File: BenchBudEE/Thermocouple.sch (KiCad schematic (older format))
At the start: 0 parts

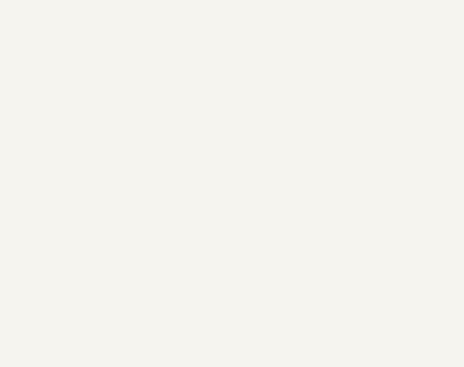
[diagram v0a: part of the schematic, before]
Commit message: Added initial module I/O
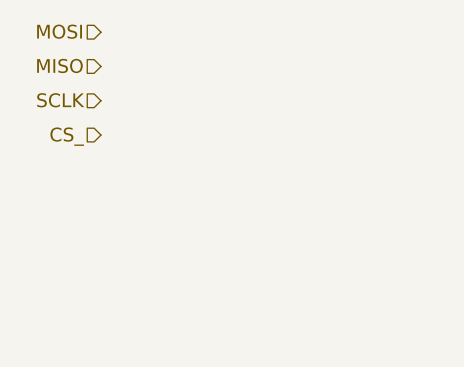
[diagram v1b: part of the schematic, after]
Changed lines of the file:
@@
 Text HLabel 9450 2900 2    60   Input ~ 0
 TC IN-
+Text HLabel 1300 1700 0    60   Input ~ 0
+MISO
+Text HLabel 1300 1550 0    60   Input ~ 0
+MOSI
+Text HLabel 1300 1850 0    60   Input ~ 0
+SCLK
+Text HLabel 1300 2000 0    60   Input ~ 0
+CS_
 $EndSCHEMATC

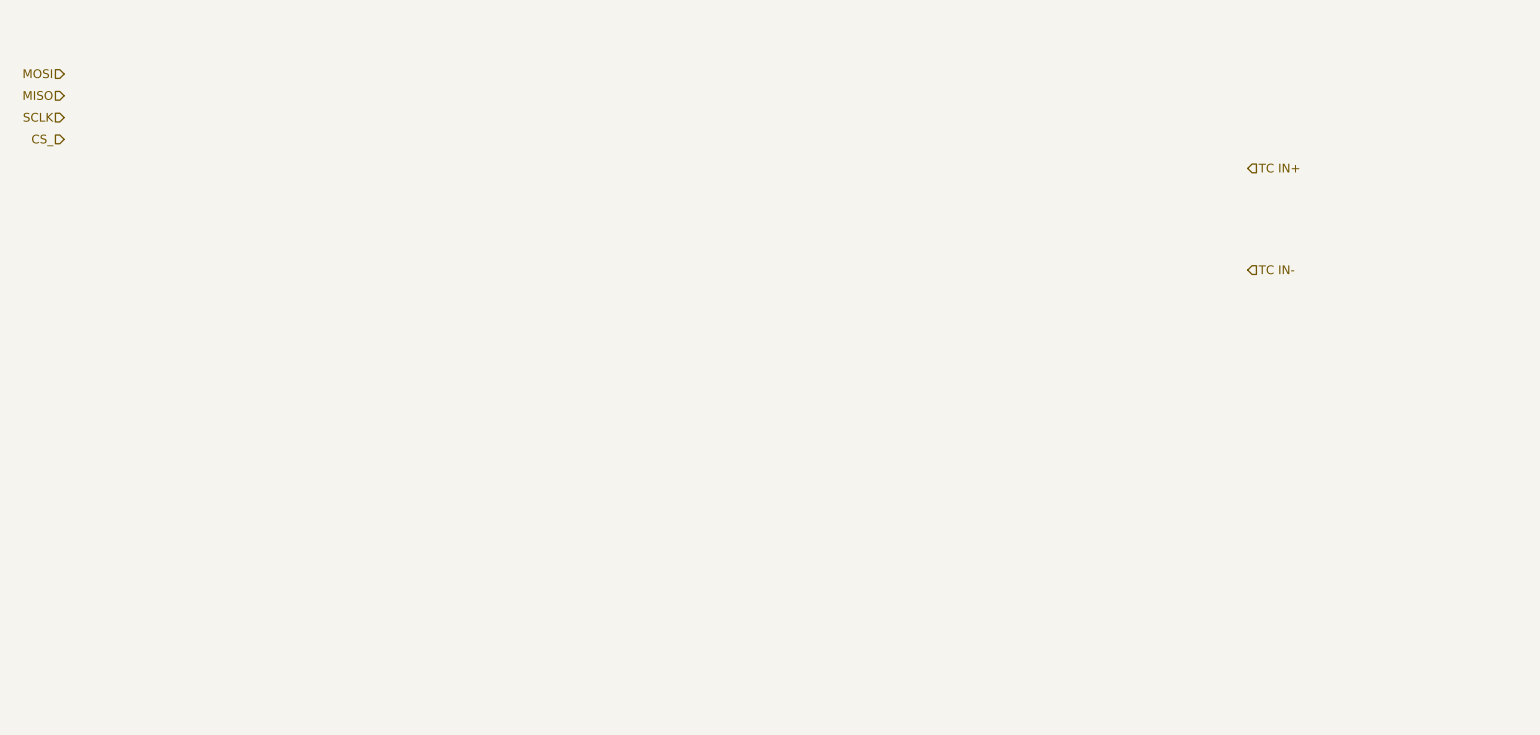
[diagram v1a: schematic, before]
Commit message: Created thermocouple module block diagram
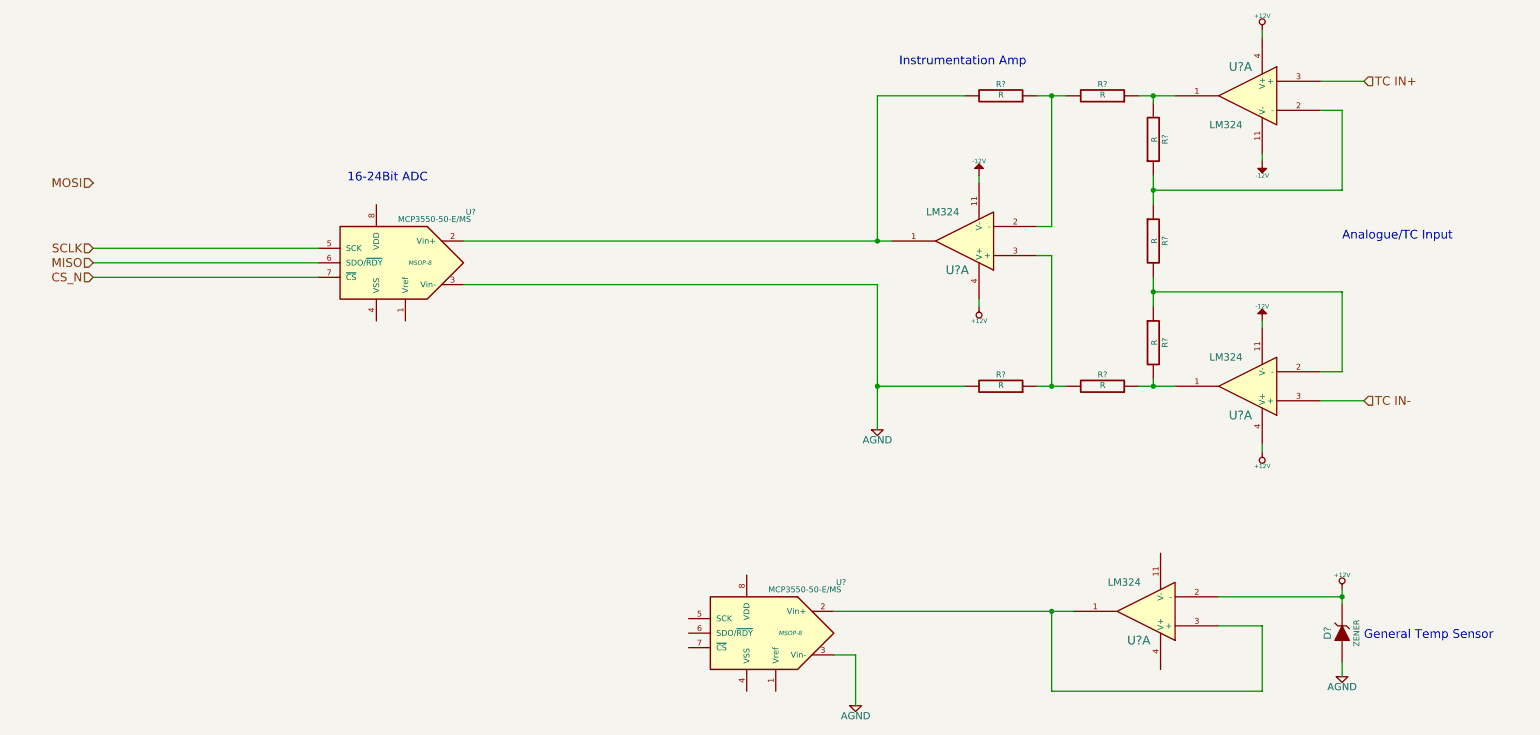
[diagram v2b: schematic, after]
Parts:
- added D?: ZENER, ~, symbol ZENER
- added R? (x7): R, ~, symbol R
- added U? (x4): LM324, symbol LM324
- added U? (x2): MCP3550-50-E/MS, MSOP-8, symbol MCP3550-50-E/MS
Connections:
- net MISO: now also U?.6 (SDO/~RDY~)
- net SCLK: now also U?.5 (SCK)
- net TC IN+: now also U?.3 (+)
- net TC IN-: now also U?.3 (+)
- new net: R?.1, R?.2, U?.2 (-) (x2)
- new net: R?.1, R?.2, U?.1 (x2)
- new net: R?.1, R?.1, U?.2 (-)
- new net: R?.2, U?.1, U?.2 (Vin+)
- new net: R?.1, R?.2, U?.3 (+)
- new net: U?.1, U?.2 (Vin+), U?.3 (+)
- new net +12V: D?.2 (K), U?.2 (-), U?.4 (V+), U?.4 (V+), U?.4 (V+)
- new net -12V: U?.11 (V-), U?.11 (V-), U?.11 (V-)
- new net AGND: D?.1 (A), R?.2, U?.3 (Vin-), U?.3 (Vin-)
- new net CS_N: U?.7 (~CS~)
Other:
- note added: "16-24Bit ADC"
- note added: "Analogue/TC Input"
- note added: "General Temp Sensor"
- note added: "Instrumentation Amp"

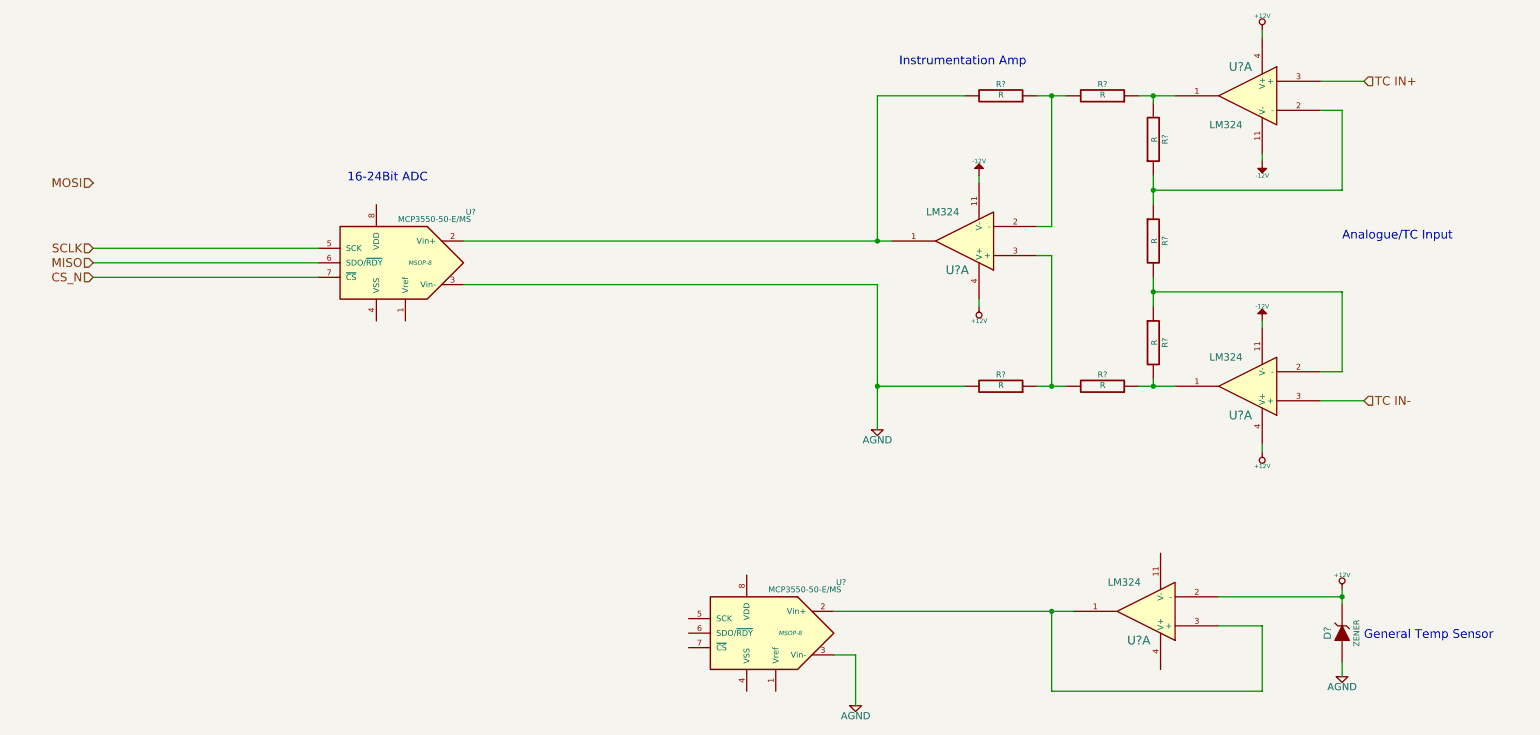
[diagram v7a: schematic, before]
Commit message: Design rules specified for layout.
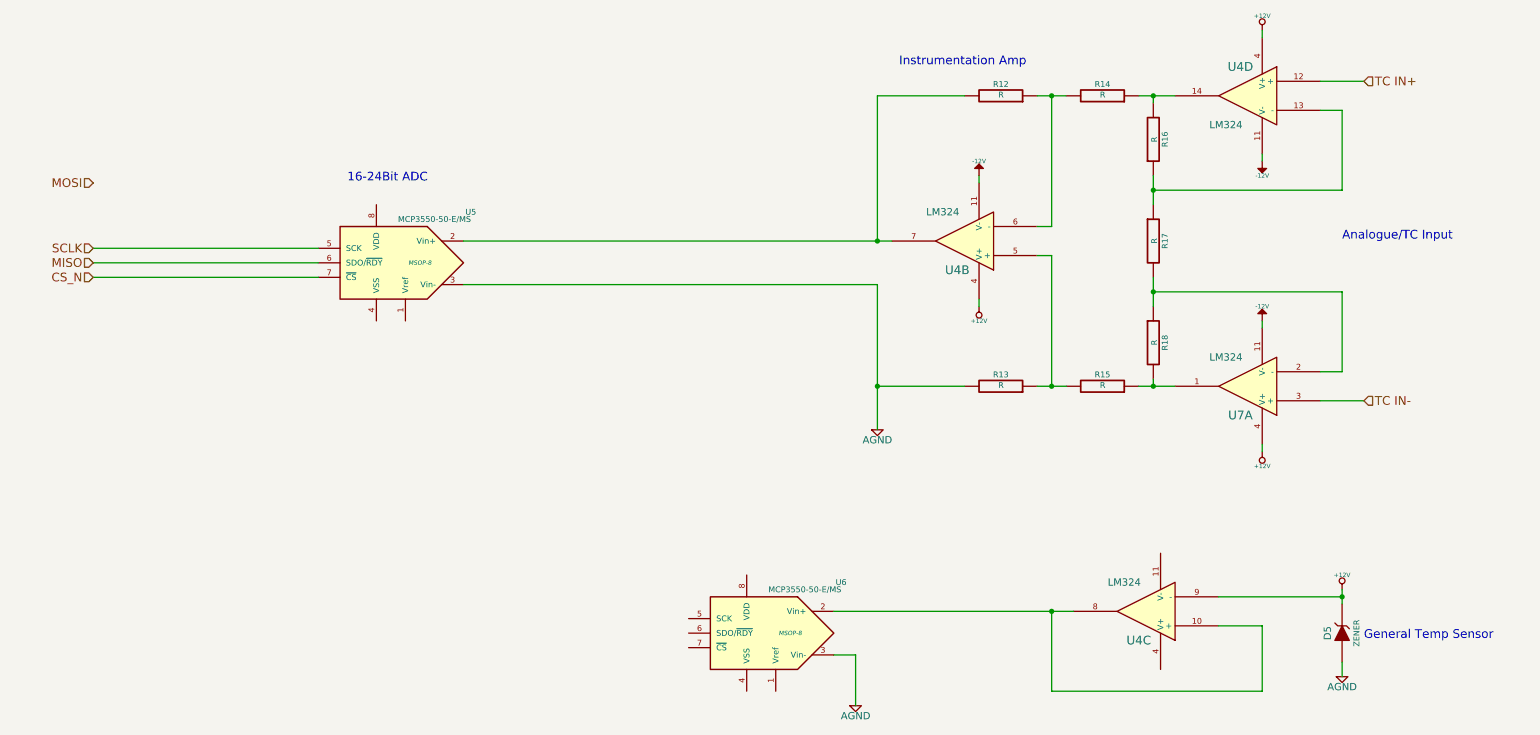
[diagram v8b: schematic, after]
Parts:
- gave numbers to parts that had none: 12
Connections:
- net +12V: now also U4.9 (-); no longer U4.2 (-)
- net TC IN+: now also U4.12 (+); no longer U4.3 (+)
- net at R14.1, R16.2: now also U4.14; no longer U4.1
- net at R16.1, R17.1: now also U4.13 (-); no longer U4.2 (-)
- net at R12.2, U5.2 (Vin+): now also U4.7; no longer U4.1
- net at R12.1, R14.2: now also U4.6 (-); no longer U4.2 (-)
- net at R13.1, R15.2: now also U4.5 (+); no longer U4.3 (+)
- new net: U4.10 (+), U4.8, U6.2 (Vin+)
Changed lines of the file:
@@
 CS_N
 $Comp
-L R R?
+L R R18
 U 1 1 52F17BC8
 P 8800 3400
-F 0 "R?" V 8880 3400 40  0000 C CNN
+F 0 "R18" V 8880 3400 40  0000 C CNN
 F 1 "R" V 8807 3401 40  0000 C CNN
 F 2 "~" V 8730 3400 30  0000 C CNN
@@
 $EndComp
 $Comp
-L LM324 U?
-U 1 1 52F17BD7
+L LM324 U4
+U 4 1 52F17BD7
 P 9450 1700
-F 0 "U?" H 9500 1900 60  0000 C CNN
+F 0 "U4" H 9500 1900 60  0000 C CNN
 F 1 "LM324" H 9600 1500 50  0000 C CNN
 F 2 "" H 9450 1700 60  0000 C CNN
 F 3 "" H 9450 1700 60  0000 C CNN
-	1    9450 1700
+	4    9450 1700
 	-1   0    0    -1
 $EndComp
 $Comp
-L LM324 U?
+L LM324 U7
 U 1 1 52F17BE4
 P 9450 3700
-F 0 "U?" H 9500 3900 60  0000 C CNN
+F 0 "U7" H 9500 3900 60  0000 C CNN
 F 1 "LM324" H 9600 3500 50  0000 C CNN
 F 2 "" H 9450 3700 60  0000 C CNN
@@
 $EndComp
 $Comp
-L R R?
+L R R17
 U 1 1 52F17BF9
 P 8800 2700
-F 0 "R?" V 8880 2700 40  0000 C CNN
+F 0 "R17" V 8880 2700 40  0000 C CNN
 F 1 "R" V 8807 2701 40  0000 C CNN
 F 2 "~" V 8730 2700 30  0000 C CNN
@@
 $EndComp
 $Comp
-L R R?
+L R R16
 U 1 1 52F17BFF
 P 8800 2000
-F 0 "R?" V 8880 2000 40  0000 C CNN
+F 0 "R16" V 8880 2000 40  0000 C CNN
 F 1 "R" V 8807 2001 40  0000 C CNN
 F 2 "~" V 8730 2000 30  0000 C CNN
@@
 $EndComp
 $Comp
-L LM324 U?
-U 1 1 52F17C19
+L LM324 U4
+U 2 1 52F17C19
 P 7500 2700
-F 0 "U?" H 7550 2900 60  0000 C CNN
+F 0 "U4" H 7550 2900 60  0000 C CNN
 F 1 "LM324" H 7650 2500 50  0000 C CNN
 F 2 "" H 7500 2700 60  0000 C CNN
 F 3 "" H 7500 2700 60  0000 C CNN
-	1    7500 2700
+	2    7500 2700
 	-1   0    0    1
 $EndComp
 $Comp
-L R R?
+L R R14
 U 1 1 52F17C38
 P 8450 1700
-F 0 "R?" V 8530 1700 40  0000 C CNN
+F 0 "R14" V 8530 1700 40  0000 C CNN
 F 1 "R" V 8457 1701 40  0000 C CNN
 F 2 "~" V 8380 1700 30  0000 C CNN
@@
 $EndComp
 $Comp
-L R R?
+L R R12
 U 1 1 52F17C3E
 P 7750 1700
-F 0 "R?" V 7830 1700 40  0000 C CNN
+F 0 "R12" V 7830 1700 40  0000 C CNN
 F 1 "R" V 7757 1701 40  0000 C CNN
 F 2 "~" V 7680 1700 30  0000 C CNN
@@
 $EndComp
 $Comp
-L R R?
+L R R15
 U 1 1 52F17C4E
 P 8450 3700
-F 0 "R?" V 8530 3700 40  0000 C CNN
+F 0 "R15" V 8530 3700 40  0000 C CNN
 F 1 "R" V 8457 3701 40  0000 C CNN
 F 2 "~" V 8380 3700 30  0000 C CNN
@@
 $EndComp
 $Comp
-L R R?
+L R R13
 U 1 1 52F17C54
 P 7750 3700
-F 0 "R?" V 7830 3700 40  0000 C CNN
+F 0 "R13" V 7830 3700 40  0000 C CNN
 F 1 "R" V 7757 3701 40  0000 C CNN
 F 2 "~" V 7680 3700 30  0000 C CNN
@@
 Connection ~ 8100 3700
 $Comp
-L LM324 U?
-U 1 1 52F17F3E
+L LM324 U4
+U 3 1 52F17F3E
 P 8750 5250
-F 0 "U?" H 8800 5450 60  0000 C CNN
+F 0 "U4" H 8800 5450 60  0000 C CNN
 F 1 "LM324" H 8900 5050 50  0000 C CNN
 F 2 "" H 8750 5250 60  0000 C CNN
 F 3 "" H 8750 5250 60  0000 C CNN
-	1    8750 5250
+	3    8750 5250
 	-1   0    0    1
 $EndComp
@@
 	7500 3700 6900 3700
 $Comp
-L -12V #PWR?
+L -12V #PWR34
 U 1 1 52F17FFA
 P 9550 3250
-F 0 "#PWR?" H 9550 3380 20  0001 C CNN
+F 0 "#PWR34" H 9550 3380 20  0001 C CNN
 F 1 "-12V" H 9550 3350 30  0000 C CNN
 F 2 "" H 9550 3250 60  0000 C CNN
@@
 $EndComp
 $Comp
-L -12V #PWR?
+L -12V #PWR33
 U 1 1 52F18007
 P 9550 2150
-F 0 "#PWR?" H 9550 2280 20  0001 C CNN
+F 0 "#PWR33" H 9550 2280 20  0001 C CNN
 F 1 "-12V" H 9550 2250 30  0000 C CNN
 F 2 "" H 9550 2150 60  0000 C CNN
@@
 $EndComp
 $Comp
-L -12V #PWR?
+L -12V #PWR30
 U 1 1 52F1800D
 P 7600 2250
-F 0 "#PWR?" H 7600 2380 20  0001 C CNN
+F 0 "#PWR30" H 7600 2380 20  0001 C CNN
 F 1 "-12V" H 7600 2350 30  0000 C CNN
 F 2 "" H 7600 2250 60  0000 C CNN
@@
 	9550 3300 9550 3250
 $Comp
-L +12V #PWR?
+L +12V #PWR35
 U 1 1 52F18082
 P 9550 4150
-F 0 "#PWR?" H 9550 4100 20  0001 C CNN
+F 0 "#PWR35" H 9550 4100 20  0001 C CNN
 F 1 "+12V" H 9550 4250 30  0000 C CNN
 F 2 "" H 9550 4150 60  0000 C CNN
@@
 $EndComp
 $Comp
-L +12V #PWR?
+L +12V #PWR32
 U 1 1 52F1808F
 P 9550 1250
-F 0 "#PWR?" H 9550 1200 20  0001 C CNN
+F 0 "#PWR32" H 9550 1200 20  0001 C CNN
 F 1 "+12V" H 9550 1350 30  0000 C CNN
 F 2 "" H 9550 1250 60  0000 C CNN
@@
 $EndComp
 $Comp
-L +12V #PWR?
+L +12V #PWR31
 U 1 1 52F18095
 P 7600 3150
-F 0 "#PWR?" H 7600 3100 20  0001 C CNN
+F 0 "#PWR31" H 7600 3100 20  0001 C CNN
 F 1 "+12V" H 7600 3250 30  0000 C CNN
 F 2 "" H 7600 3150 60  0000 C CNN
@@
 	9550 1300 9550 1250
 $Comp
-L MCP3550-50-E/MS U?
+L MCP3550-50-E/MS U5
 U 1 1 52F18159
 P 3550 2850
-F 0 "U?" H 3000 3200 40  0000 C CNN
+F 0 "U5" H 3000 3200 40  0000 C CNN
 F 1 "MCP3550-50-E/MS" H 3250 3150 40  0000 C CNN
 F 2 "MSOP-8" H 3350 2850 30  0000 C CIN
@@
 	1500 2750 3050 2750
 $Comp
-L MCP3550-50-E/MS U?
+L MCP3550-50-E/MS U6
 U 1 1 52F18264
 P 6100 5400
-F 0 "U?" H 5550 5750 40  0000 C CNN
+F 0 "U6" H 5550 5750 40  0000 C CNN
 F 1 "MCP3550-50-E/MS" H 5800 5700 40  0000 C CNN
 F 2 "MSOP-8" H 5900 5400 30  0000 C CIN
@@
 $EndComp
 $Comp
-L ZENER D?
+L ZENER D5
 U 1 1 52F18276
 P 10100 5400
-F 0 "D?" H 10100 5500 50  0000 C CNN
+F 0 "D5" H 10100 5500 50  0000 C CNN
 F 1 "ZENER" H 10100 5300 40  0000 C CNN
 F 2 "~" H 10100 5400 60  0000 C CNN
@@
 $EndComp
 $Comp
-L +12V #PWR?
+L +12V #PWR36
 U 1 1 52F18283
 P 10100 5100
-F 0 "#PWR?" H 10100 5050 20  0001 C CNN
+F 0 "#PWR36" H 10100 5050 20  0001 C CNN
 F 1 "+12V" H 10100 5200 30  0000 C CNN
 F 2 "" H 10100 5100 60  0000 C CNN
@@
 General Temp Sensor
 $Comp
-L AGND #PWR?
+L AGND #PWR29
 U 1 1 52F183E0
 P 6900 4000
-F 0 "#PWR?" H 6900 4000 40  0001 C CNN
+F 0 "#PWR29" H 6900 4000 40  0001 C CNN
 F 1 "AGND" H 6900 3930 50  0000 C CNN
 F 2 "" H 6900 4000 60  0000 C CNN
@@
 	6900 3000 6900 4000
 $Comp
-L AGND #PWR?
+L AGND #PWR37
 U 1 1 52F18458
 P 10100 5700
-F 0 "#PWR?" H 10100 5700 40  0001 C CNN
+F 0 "#PWR37" H 10100 5700 40  0001 C CNN
 F 1 "AGND" H 10100 5630 50  0000 C CNN
 F 2 "" H 10100 5700 60  0000 C CNN
@@
 	10100 5600 10100 5700
 $Comp
-L AGND #PWR?
+L AGND #PWR28
 U 1 1 52F18493
 P 6750 5900
-F 0 "#PWR?" H 6750 5900 40  0001 C CNN
+F 0 "#PWR28" H 6750 5900 40  0001 C CNN
 F 1 "AGND" H 6750 5830 50  0000 C CNN
 F 2 "" H 6750 5900 60  0000 C CNN
